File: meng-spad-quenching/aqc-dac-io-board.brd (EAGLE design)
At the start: 101.6 x 101.6 mm, 34 parts, among them IC1 LT1366, IC2 74LVT126, IC4 MAX1680, X1 CONN_VREF_CASCODE_IBIAS, X2 CONN_VREF_DIAMOND_IBIAS, X3 CONN_VREF_ONE_SHOT, X4 CONN_PHOTON_COUNTER, X5 CONN_FORCE_QUENCH

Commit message: Work on layout
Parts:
- moved C1 78.7 mm to (12.1, 93.0), turned to 90 degrees
- moved C6 77.6 mm to (19.7, 98.7)
- moved C2 74.1 mm to (14.3, 93.0), turned to 90 degrees
- moved R2 70.8 mm to (21.9, 69.5)
- moved C7 70.3 mm to (25.4, 94.9), turned to 90 degrees
- moved R3 70.3 mm to (21.9, 71.8)
- moved IC4 65.6 mm to (19.7, 94.3), turned to 90 degrees
- moved STM32_NUCLEO 53.4 mm to (31.8, 24.1), turned to 90 degrees
- moved H2 50.8 mm to (47.0, 97.8)
- moved H4 50.8 mm to (47.0, 3.81)
- moved U1 20.1 mm to (13.0, 69.2)
- moved U2 20.1 mm to (13.0, 60.3)
- moved C3 20.1 mm to (13.7, 66.0)
- moved C4 20.1 mm to (13.7, 57.1)
- moved U3 20.0 mm to (13.0, 52.1)
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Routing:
- net DAC_SCL: track 0.00 -> 30.4 mm
- net N$7: track 2.89 -> 17.5 mm
- net N$1: track 0.00 -> 9.51 mm
- net N$5: track 3.41 -> 11.7 mm
- net FORCE_QUENCH_BUF: track 10.4 -> 7.85 mm
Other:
- board size 101.6 x 101.6 mm -> 50.8 x 101.6 mm

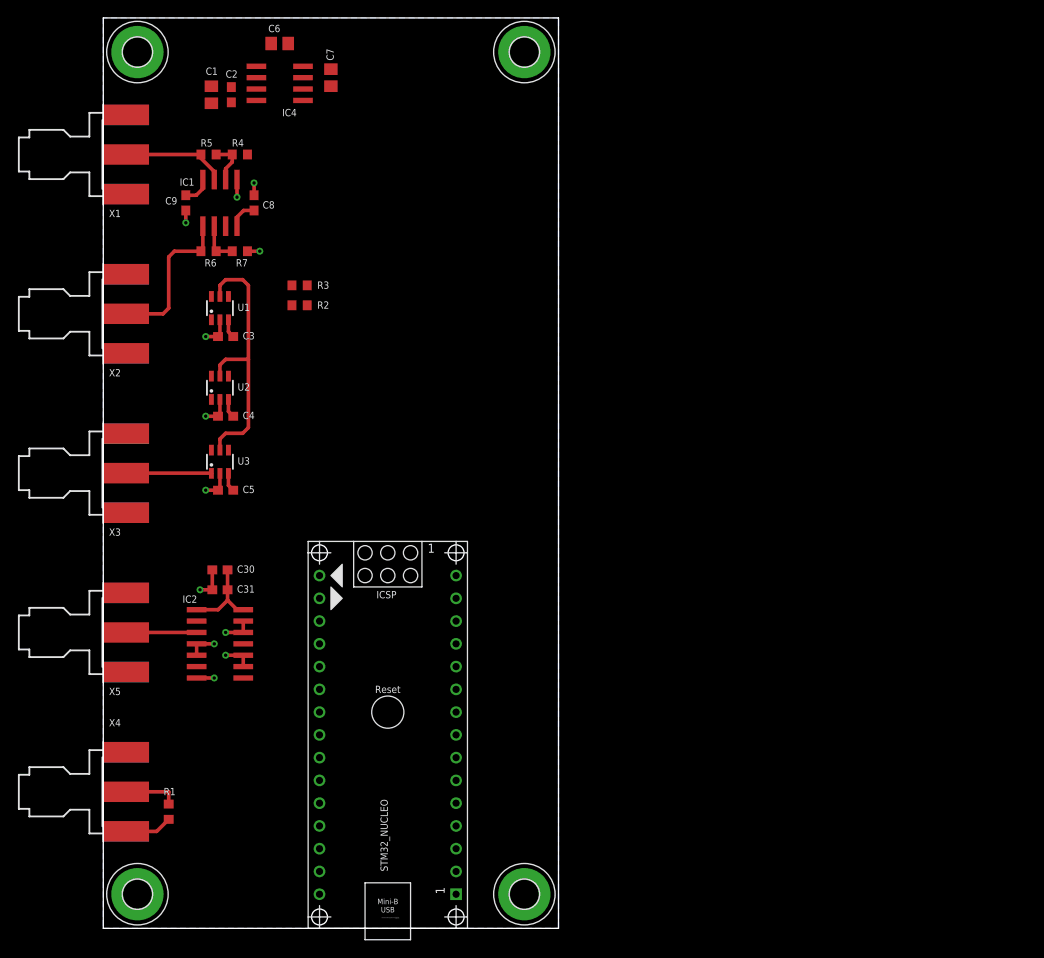
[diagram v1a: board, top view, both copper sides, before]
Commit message: Added DIO MCU connections, placed and routed 1st pass
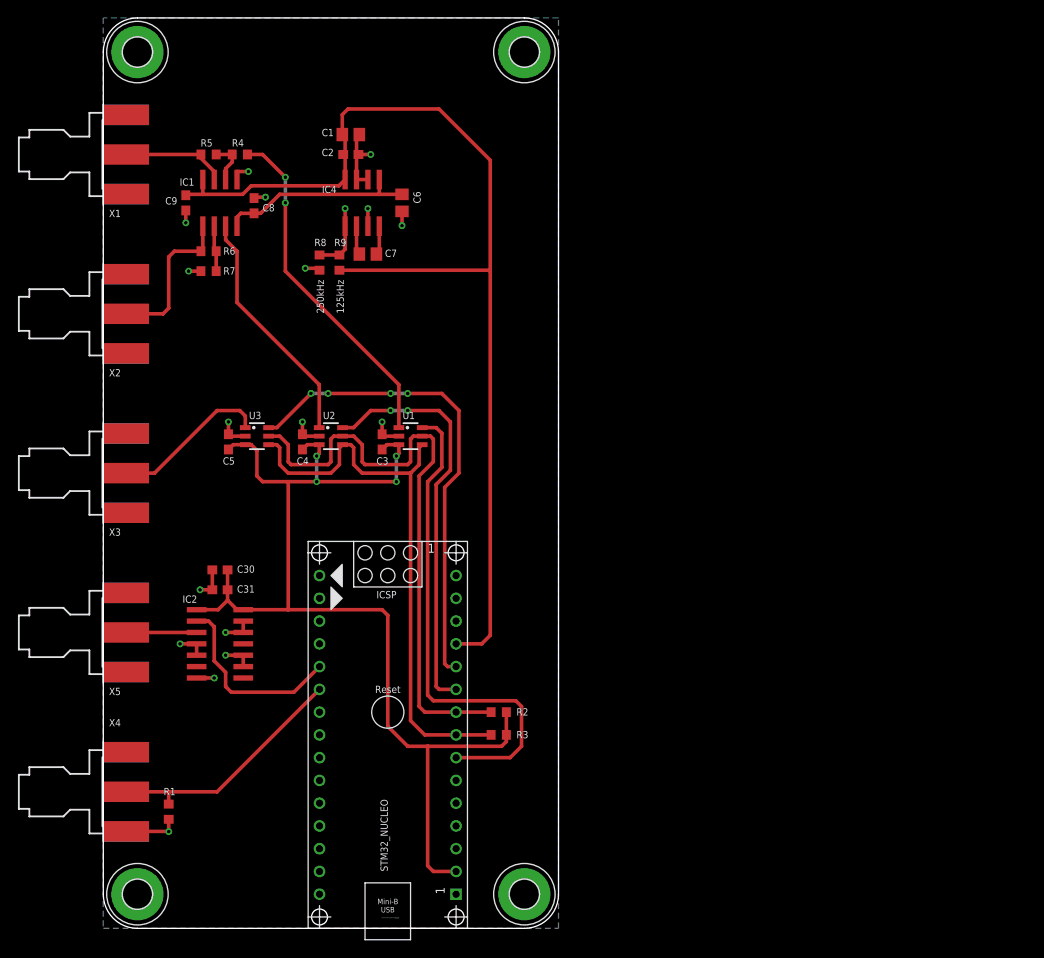
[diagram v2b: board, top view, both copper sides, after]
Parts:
- added R8: 0R, resistor:R0603
- added R9: DNP, resistor:R0603
- moved R3 54.9 mm to (44.1, 21.6)
- moved R2 50.6 mm to (44.1, 24.1)
- moved U1 25.6 mm to (34.3, 54.9), turned to 270 degrees
- moved C6 22.4 mm to (33.3, 81.0), turned to 270 degrees
- moved C3 21.0 mm to (31.1, 54.3), turned to 90 degrees
- moved C7 20.1 mm to (29.5, 75.2), turned to 0 degrees
- moved IC4 16.2 mm to (28.9, 81.0), turned to 0 degrees
- moved C1 16.2 mm to (27.6, 88.6), turned to 0 degrees
- moved C2 14.9 mm to (27.6, 86.4), turned to 0 degrees
- moved U2 13.5 mm to (25.4, 54.9), turned to 270 degrees
- moved C4 9.04 mm to (22.2, 54.3), turned to 90 degrees
- moved C5 5.41 mm to (14.0, 54.3), turned to 90 degrees
- moved U3 5.02 mm to (17.1, 54.9), turned to 270 degrees
- moved R7 4.14 mm to (11.7, 73.3), turned to 0 degrees
- moved C8 0.32 mm to (16.8, 80.6)
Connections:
- new net N$4: IC4.1, R8.2, R9.1
- net DAC_CASCODE_IBIAS_SEL: now also STM32_NUCLEO.7
- net DAC_DIAMOND_IBIAS_SEL: now also STM32_NUCLEO.10
- net DAC_ONE_SHOT_SEL: now also STM32_NUCLEO.11
- net FORCE_QUENCH_MCU: now also STM32_NUCLEO.20
- net GND: now also R8.1; no longer IC4.1
- net PHOTON_COUNTER: now also STM32_NUCLEO.21
- net PP_P5V0: now also R9.2
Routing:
- net PP_P5V0: track 3.22 -> 121.0 mm
- net PP_P3V3: track 15.8 -> 122.0 mm, vias 0 -> 4
- net DAC_SDA: track 0.00 -> 64.1 mm
- net DAC_CASCODE_IBIAS_SEL: track 0.00 -> 55.6 mm
- net DAC_ONE_SHOT_SEL: track 0.00 -> 53.9 mm, vias 0 -> 4
- net DAC_DIAMOND_IBIAS_SEL: track 0.00 -> 45.9 mm, vias 0 -> 2
- net N$2: track 0.00 -> 38.5 mm, vias 0 -> 2
- net DAC_SCL: track 30.4 -> 67.8 mm
- net N$6: track 0.00 -> 26.8 mm
- net PHOTON_COUNTER: track 6.11 -> 27.7 mm
- net FORCE_QUENCH_MCU: track 0.00 -> 21.3 mm
- net PP_N5V0: track 3.22 -> 22.1 mm
- net GND: track 36.7 -> 50.7 mm, vias 12 -> 17
- net N$1: track 9.51 -> 17.7 mm
- net N$4: track 0.00 -> 7.67 mm, vias 0 -> 1
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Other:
- outline, holes or cut-outs redrawn
- board text added: "125kHz"
- board text added: "250kHz"

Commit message: Exported gerbers and BOM
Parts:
- removed C30: 100n, rcl:C0603
- removed C31: 10n, rcl:C0603
- added C10: 100n, rcl:C0603
- added C11: 4u7, rcl:C0805
- added R10, R11: 2k2, resistor:R0603
- added TP1: PP_P5V0, Kramnik's Library:KEYSTONE_5000_MINIATURE
- added TP2: GND, Kramnik's Library:KEYSTONE_5000_MINIATURE
- added TP3: PP_N5V0, Kramnik's Library:KEYSTONE_5000_MINIATURE
- C1, C6: value 4u7 -> 100n; device rcl:C0805 -> rcl:C0603
- C4: value 100n -> 10n
- C9: value 100n -> 4u7; device rcl:C0603 -> rcl:C0805
- R1: value 49R9 -> 100R
- R2: value 2k2 -> 100R
- R3: value 2k2 -> 15k0
- R4: value 10k0 -> 5k11
- R5: value 15k0 -> 10k0
- R6: value 5k11 -> 10k0
- R7: value 10k0 -> 0R
- R8: value 0R -> DNP
- R9: value DNP -> 0R
- X4: value CONN_PHOTON_COUNTER -> CONN_FORCE_QUENCH
- X5: value CONN_FORCE_QUENCH -> CONN_PHOTON_COUNTER
- moved H2 103.4 mm to (3.81, 3.81)
- moved H3 103.4 mm to (47.0, 97.8)
- moved R3 72.4 mm to (11.7, 86.4)
- moved R2 36.3 mm to (9.53, 13.0), turned to 90 degrees
- moved C2 35.5 mm to (12.4, 54.3), turned to 90 degrees
- moved C6 29.5 mm to (20.6, 54.3), turned to 90 degrees
- moved C5 26.5 mm to (16.8, 80.6)
- moved C3 23.1 mm to (13.0, 40.0), turned to 180 degrees
- moved C9 21.1 mm to (29.5, 75.2), turned to 0 degrees
- moved C1 19.9 mm to (9.21, 81.0), turned to 270 degrees
- moved C4 18.9 mm to (13.0, 37.8), turned to 180 degrees
- moved U1 18.7 mm to (15.6, 54.9)
- moved X4 17.8 mm to (0.00, 33.0)
- moved X5 17.8 mm to (0.00, 15.2)
- moved R9 17.3 mm to (43.2, 70.5)
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- renumbered IC4 to IC3
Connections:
- new net N$9: R9.2, STM32_NUCLEO.12
- net DAC_CASCODE_IBIAS_SEL: now also U3.6; no longer U1.6
- net DAC_ONE_SHOT_SEL: now also U1.6; no longer U3.6
- net DAC_SCL: now also R10.1; no longer R2.1
- net DAC_SDA: now also R11.1; no longer R3.1
- net FORCE_QUENCH_BUF: now also X4.1; no longer X5.1
- net GND: now also C10.2, C11.2, C7.2, R2.1, R5.1, TP2.P$1; no longer C30.2, C31.2, C9.2, R8.1
- net N$1: now also U1.1; no longer U3.1
- net N$14: now also C9.2; no longer C7.2
- net N$15: now also C9.1; no longer C7.1
- net N$2: now also R6.2, U3.1; no longer R4.2, U1.1
- net N$3: now also R3.2, R6.1; no longer R4.1, R5.2
- net N$4: now also R7.2, R8.1; no longer R8.2, R9.1
- net N$5: now also R3.1; no longer R5.1
- net N$7: now also R4.2; no longer R6.2
- net N$8: now also R4.1, R5.2; no longer R6.1, R7.2
- net PHOTON_COUNTER: now also R2.2, X5.1; no longer X4.1
- net PP_N5V0: now also C11.1, C5.1, TP3.P$1; no longer C6.1, C8.1
- net PP_P3V3: now also C10.1, C2.1, C6.1, R10.2, R11.2; no longer C30.1, C31.1, C5.1, R2.2, R3.2
- net PP_P5V0: now also C7.1, C8.1, R8.2, R9.1, TP1.P$1; no longer C2.1, C9.1, R9.2, STM32_NUCLEO.12
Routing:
- net PP_P5V0: track 121.0 -> 80.2 mm
- net N$9: track 0.00 -> 39.5 mm
- net PP_N5V0: track 22.1 -> 28.2 mm
- net DAC_CASCODE_IBIAS_SEL: track 55.6 -> 59.0 mm
- net PP_P3V3: track 122.0 -> 124.2 mm
- net DAC_SDA: track 64.1 -> 66.2 mm
- net GND: track 50.7 -> 52.6 mm
- net N$1: track 17.7 -> 19.5 mm
- net PHOTON_COUNTER: track 27.7 -> 29.0 mm
- net DAC_DIAMOND_IBIAS_SEL: track 45.9 -> 44.9 mm
- net DAC_ONE_SHOT_SEL: track 53.9 -> 53.1 mm
- net DAC_SCL: track 67.8 -> 68.6 mm
- net N$6: track 26.8 -> 26.2 mm
- net N$2: track 38.5 -> 37.8 mm
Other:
- board text added: "AQC DAC IO Board Rev. 1"
- board text added: "Spring 2017"
- board text added: "kramnik@mit.edu"
- board text added: "rajeev@mit.edu"

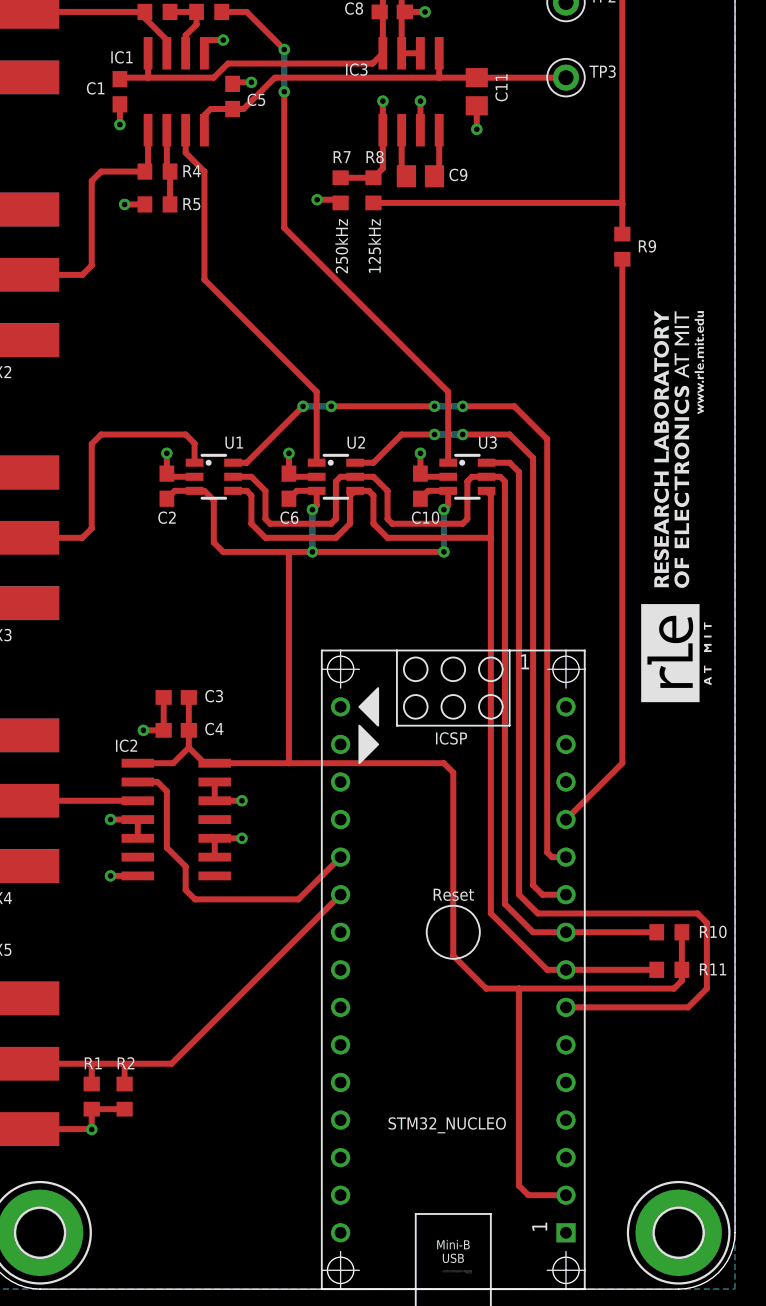
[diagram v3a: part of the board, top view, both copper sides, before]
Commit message: Added debounced trigger switch, routed, and exported gerbers
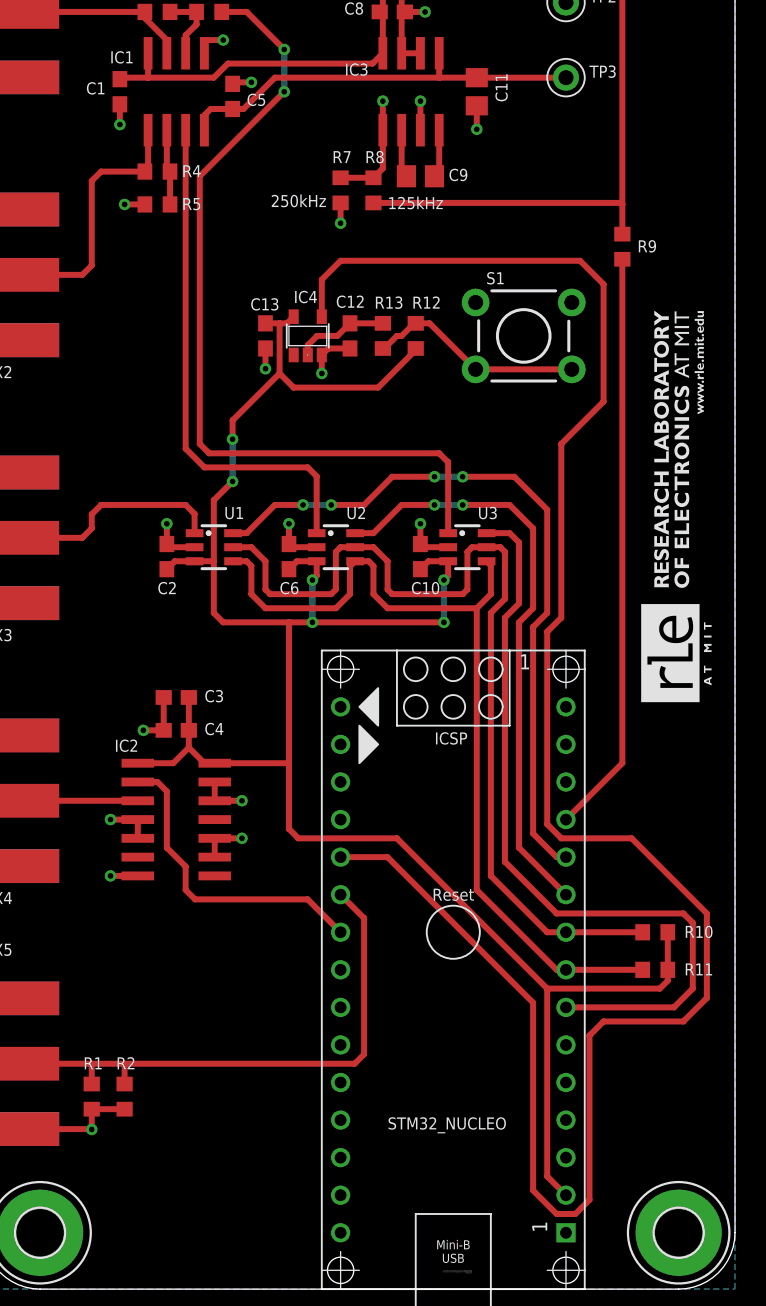
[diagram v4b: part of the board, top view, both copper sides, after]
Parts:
- added C12, C13: 100n, rcl:C0603
- added IC4: 74AHC1G14DBV, 74xx-little-us:SOT23-5
- added R12: 4k7, resistor:R0603
- added R13: 100k, resistor:R0603
- added S1: (no value), Kramnik's Library:TACTILE-PTH
- U1, U2, U3: value (none) -> MCP4725
- moved U1 4.76 mm to (15.6, 50.2)
- moved U2 4.76 mm to (23.8, 50.2)
- moved U3 4.76 mm to (32.7, 50.2)
- moved C10 4.76 mm to (29.5, 49.5)
- moved C2 4.76 mm to (12.4, 49.5)
- moved C6 4.76 mm to (20.6, 49.5)
- moved R10 0.95 mm to (45.4, 24.1)
- moved R11 0.95 mm to (45.4, 21.6)
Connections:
- new net N$11: R12.1, R13.2, S1.3, S1.4
- new net N$12: C12.1, IC4.2, R13.1
- new net TRIGGER_BTN: IC4.4, STM32_NUCLEO.20
- net FORCE_QUENCH_MCU: now also STM32_NUCLEO.22; no longer STM32_NUCLEO.20
- net GND: now also C12.2, C13.2, IC4.3, S1.1, S1.2
- net PP_P3V3: now also C13.1, IC4.5, R12.2
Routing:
- net TRIGGER_BTN: track 0.00 -> 134.6 mm
- net N$2: track 37.8 -> 56.4 mm
- net PP_P3V3: track 124.2 -> 142.7 mm, vias 4 -> 6
- net N$11: track 0.00 -> 14.8 mm
- net N$6: track 26.2 -> 35.0 mm
- net PHOTON_COUNTER: track 29.0 -> 37.6 mm
- net DAC_CASCODE_IBIAS_SEL: track 59.0 -> 52.4 mm
- net N$12: track 0.00 -> 6.35 mm
- net DAC_SDA: track 66.2 -> 60.0 mm
- net DAC_SCL: track 68.6 -> 63.1 mm
- net DAC_DIAMOND_IBIAS_SEL: track 44.9 -> 40.0 mm
- net N$1: track 19.5 -> 14.7 mm
- net GND: track 52.6 -> 57.0 mm, vias 17 -> 19
- net DAC_ONE_SHOT_SEL: track 53.1 -> 48.9 mm
